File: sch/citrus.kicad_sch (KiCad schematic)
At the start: 1 part, among them J2 ERF8-025-05.0-L-DV-L-K-TR

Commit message: added tps and new init layout
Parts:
- renumbered J2 to J3
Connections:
- net GND: now also J3.03, J3.05, J3.16, J3.18, J3.24, J3.26, J3.32, J3.34, J3.40, J3.42
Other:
- moved on the sheet: J3

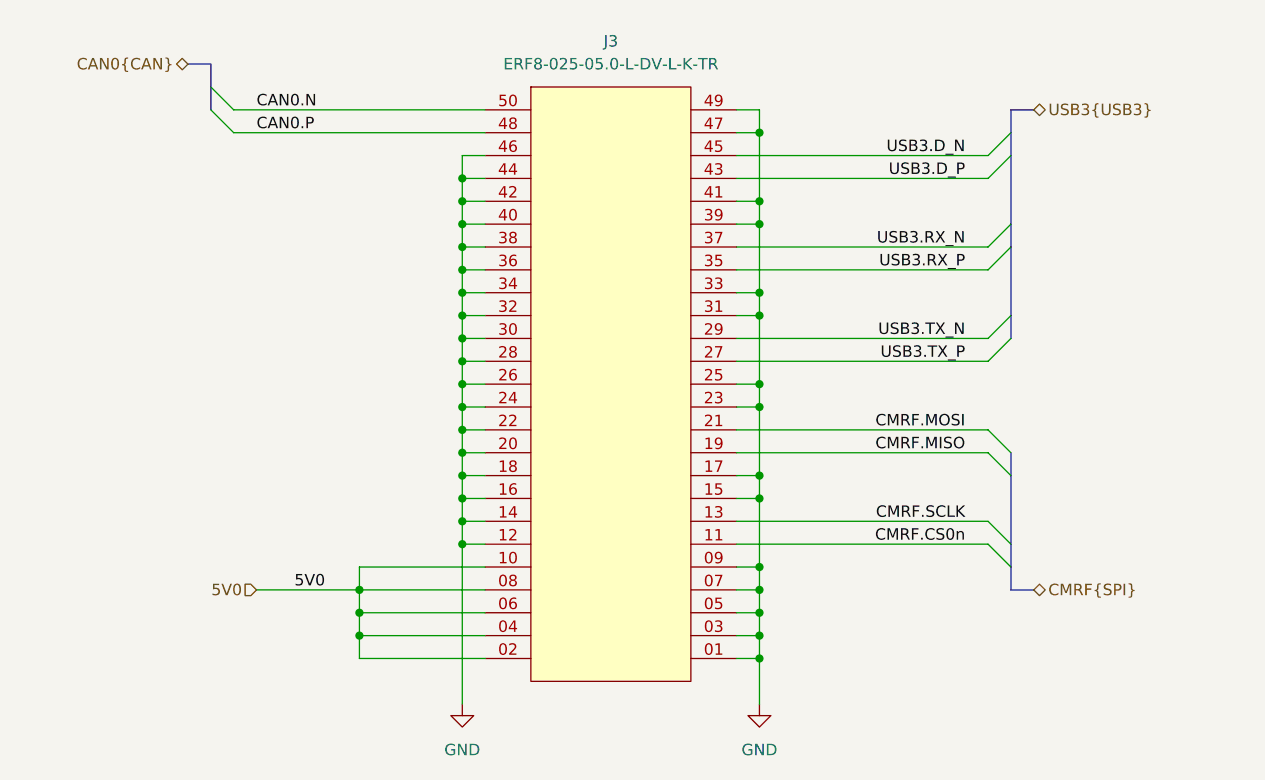
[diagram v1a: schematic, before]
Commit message: rev b, flipped connectors
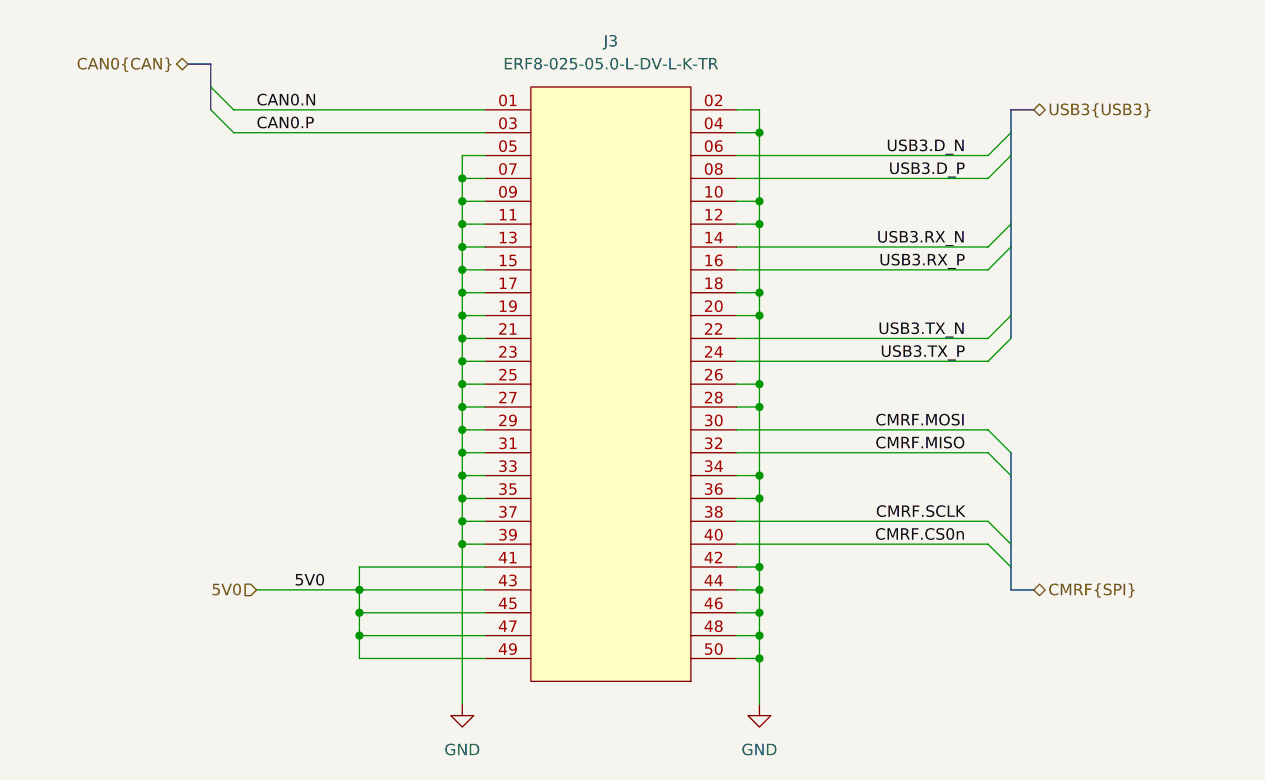
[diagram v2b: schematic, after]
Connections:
- net 5V0: now also J3.41, J3.43, J3.45, J3.47, J3.49; no longer J3.02, J3.04, J3.06, J3.08, J3.10
- net CAN0.N: now also J3.01; no longer J3.50
- net CAN0.P: now also J3.03; no longer J3.48
- net CMRF.CS0n: now also J3.40; no longer J3.11
- net CMRF.MISO: now also J3.32; no longer J3.19
- net CMRF.MOSI: now also J3.30; no longer J3.21
- net CMRF.SCLK: now also J3.38; no longer J3.13
- net GND: now also J3.02, J3.04, J3.10, J3.11, J3.13, J3.19, J3.21, J3.27, J3.29, J3.35, J3.37, J3.48, J3.50; no longer J3.01, J3.03, J3.14, J3.16, J3.22, J3.24, J3.30, J3.32, J3.38, J3.40, J3.41, J3.47, J3.49
- net USB3.D_N: now also J3.06; no longer J3.45
- net USB3.D_P: now also J3.08; no longer J3.43
- net USB3.RX_N: now also J3.14; no longer J3.37
- net USB3.RX_P: now also J3.16; no longer J3.35
- net USB3.TX_N: now also J3.22; no longer J3.29
- net USB3.TX_P: now also J3.24; no longer J3.27
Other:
- moved on the sheet: J3
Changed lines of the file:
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@@
 	(symbol
 		(lib_id "library:ERF8-025-05.0-L-DV-L-K-TR")
-		(at 143.51 99.06 0)
+		(at 143.51 99.06 180)
 		(unit 1)
 		(body_style 1)
@@
 		(in_pos_files yes)
 		(dnp no)
-		(fields_autoplaced yes)
 		(property "Reference" "J3"
 			(at 143.51 60.96 0)
